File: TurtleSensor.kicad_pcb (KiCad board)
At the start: 2 copper layers, 72 x 72 mm, 10 parts, among them IC1 ATMEGA328-P, U1 HTU21DBreakout, U2 W25Q32FlashBreakout

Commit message: started routing
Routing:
- net +BATT: track 0.00 -> 114.0 mm
- net /SDA: track 0.00 -> 29.1 mm
- net /MOSI: track 0.00 -> 23.0 mm
- net /SCL: track 0.00 -> 18.5 mm
- net Net-(D1-Pad2): track 0.00 -> 15.7 mm
- net /MISO: track 0.00 -> 15.4 mm
- net /~CS: track 0.00 -> 14.4 mm
- net /SCK: track 0.00 -> 14.4 mm
- net Net-(22pF1-Pad2): track 0.00 -> 12.5 mm
- net Net-(22pF2-Pad2): track 0.00 -> 12.0 mm
- net Net-(D1-Pad1): track 0.00 -> 5.84 mm
- added copper zone on F.Cu, net GND
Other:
- net class Default: trace_width 0.25 -> 0.5
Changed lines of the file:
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@@
   (general
     (links 26)
-    (no_connects 26)
+    (no_connects 8)
     (area 97 79 170 152)
     (thickness 1.6)
     (drawings 4)
-    (tracks 0)
+    (tracks 56)
     (zones 0)
     (modules 10)
@@
   )
   (setup
-    (last_trace_width 0.25)
+    (last_trace_width 0.5)
     (trace_clearance 0.2)
     (zone_clearance 0.508)
@@
   (net_class Default "This is the default net class."
     (clearance 0.2)
-    (trace_width 0.25)
+    (trace_width 0.5)
     (via_dia 0.6)
     (via_drill 0.4)
@@
   (gr_line (start 170 152) (end 98 152) (angle 90) (layer Edge.Cuts) (width 0.1))
   (gr_line (start 170 80) (end 170 152) (angle 90) (layer Edge.Cuts) (width 0.1))
+  (segment (start 112 106.55906) (end 107.05906 106.55906) (width 0.25) (layer F.Cu) (net 1) (status 400000))
+  (segment (start 107.05906 106.55906) (end 106.5 106) (width 0.25) (layer F.Cu) (net 1) (status 800000))
+  (segment (start 118 108.32) (end 113.76094 108.32) (width 0.25) (layer F.Cu) (net 1) (status 400000))
+  (segment (start 113.76094 108.32) (end 112 106.55906) (width 0.25) (layer F.Cu) (net 1) (status 800000))
+  (segment (start 118 110.86) (end 112.58094 110.86) (width 0.25) (layer F.Cu) (net 2) (status 400000))
+  (segment (start 112.58094 110.86) (end 112 111.44094) (width 0.25) (layer F.Cu) (net 2) (status 800000))
+  (segment (start 112 111.44094) (end 107.05906 111.44094) (width 0.25) (layer F.Cu) (net 2) (status 400000))
+  (segment (start 107.05906 111.44094) (end 106.5 112) (width 0.25) (layer F.Cu) (net 2) (status 800000))
+  (segment (start 141 88) (end 141 87) (width 0.25) (layer F.Cu) (net 4) (status 400000))
+  (segment (start 111 83) (end 108 86) (width 0.25) (layer F.Cu) (net 4))
+  (segment (start 137 83) (end 111 83) (width 0.25) (layer F.Cu) (net 4))
+  (segment (start 141 87) (end 137 83) (width 0.25) (layer F.Cu) (net 4))
+  (segment (start 139 105) (end 143 105) (width 0.25) (layer F.Cu) (net 4))
+  (segment (start 135.68 108.32) (end 139 105) (width 0.25) (layer F.Cu) (net 4))
+  (segment (start 125.62 108.32) (end 135.68 108.32) (width 0.25) (layer F.Cu) (net 4) (status 400000))
+  (segment (start 142 121) (end 140 121) (width 0.25) (layer F.Cu) (net 4) (status 800000))
+  (segment (start 143 120) (end 142 121) (width 0.25) (layer F.Cu) (net 4))
+  (segment (start 143 105) (end 143 120) (width 0.25) (layer F.Cu) (net 4))
+  (segment (start 125.62 105.78) (end 125.62 108.32) (width 0.25) (layer F.Cu) (net 4) (status C00000))
+  (segment (start 118 103.24) (end 123.08 103.24) (width 0.25) (layer F.Cu) (net 4) (status 400000))
+  (segment (start 123.08 103.24) (end 125.62 105.78) (width 0.25) (layer F.Cu) (net 4) (status 800000))
+  (segment (start 115 97) (end 115 102) (width 0.25) (layer F.Cu) (net 4))
+  (segment (start 114 96) (end 115 97) (width 0.25) (layer F.Cu) (net 4))
+  (segment (start 112 96) (end 114 96) (width 0.25) (layer F.Cu) (net 4) (status 400000))
+  (segment (start 116.24 103.24) (end 115 102) (width 0.25) (layer F.Cu) (net 4))
+  (segment (start 116.24 103.24) (end 118 103.24) (width 0.25) (layer F.Cu) (net 4) (status 800000))
+  (segment (start 112 96) (end 112 88) (width 0.25) (layer F.Cu) (net 4) (status 400000))
+  (segment (start 110 86) (end 112 88) (width 0.25) (layer F.Cu) (net 4))
+  (segment (start 110 86) (end 108 86) (width 0.25) (layer F.Cu) (net 4))
+  (segment (start 108 86) (end 104 86) (width 0.25) (layer F.Cu) (net 4) (status 800000))
+  (segment (start 119 132) (end 124.84 132) (width 0.25) (layer F.Cu) (net 5) (status C00000))
+  (segment (start 125.62 121.02) (end 123.98 121.02) (width 0.25) (layer F.Cu) (net 6) (status 400000))
+  (segment (start 116.46 128.54) (end 116.46 132) (width 0.25) (layer F.Cu) (net 6) (status 800000))
+  (segment (start 123.98 121.02) (end 116.46 128.54) (width 0.25) (layer F.Cu) (net 6))
+  (segment (start 125.62 118.48) (end 139.98 118.48) (width 0.25) (layer F.Cu) (net 17) (status C00000))
+  (segment (start 139.98 118.48) (end 140 118.46) (width 0.25) (layer F.Cu) (net 17) (status C00000))
+  (segment (start 125.62 115.94) (end 123.94 115.94) (width 0.25) (layer F.Cu) (net 18) (status 400000))
+  (segment (start 138.62 112) (end 140 113.38) (width 0.25) (layer F.Cu) (net 18) (status 800000))
+  (segment (start 124 112) (end 138.62 112) (width 0.25) (layer F.Cu) (net 18))
+  (segment (start 123 113) (end 124 112) (width 0.25) (layer F.Cu) (net 18))
+  (segment (start 123 115) (end 123 113) (width 0.25) (layer F.Cu) (net 18))
+  (segment (start 123.94 115.94) (end 123 115) (width 0.25) (layer F.Cu) (net 18))
+  (segment (start 140 115.92) (end 132.92 115.92) (width 0.25) (layer F.Cu) (net 19) (status 400000))
+  (segment (start 130.4 113.4) (end 125.62 113.4) (width 0.25) (layer F.Cu) (net 19) (status 800000))
+  (segment (start 132.92 115.92) (end 130.4 113.4) (width 0.25) (layer F.Cu) (net 19))
+  (segment (start 125.62 110.86) (end 139.98 110.86) (width 0.25) (layer F.Cu) (net 20) (status C00000))
+  (segment (start 139.98 110.86) (end 140 110.84) (width 0.25) (layer F.Cu) (net 20) (status C00000))
+  (segment (start 141 93.08) (end 143.08 93.08) (width 0.25) (layer F.Cu) (net 25) (status 400000))
+  (segment (start 134.08 99) (end 125.62 90.54) (width 0.25) (layer F.Cu) (net 25) (status 800000))
+  (segment (start 142 99) (end 134.08 99) (width 0.25) (layer F.Cu) (net 25))
+  (segment (start 144 97) (end 142 99) (width 0.25) (layer F.Cu) (net 25))
+  (segment (start 144 94) (end 144 97) (width 0.25) (layer F.Cu) (net 25))
+  (segment (start 143.08 93.08) (end 144 94) (width 0.25) (layer F.Cu) (net 25))
+  (segment (start 125.62 88) (end 129 88) (width 0.25) (layer F.Cu) (net 26) (status 400000))
+  (segment (start 136.62 95.62) (end 141 95.62) (width 0.25) (layer F.Cu) (net 26) (status 800000))
+  (segment (start 129 88) (end 136.62 95.62) (width 0.25) (layer F.Cu) (net 26))
+  (zone (net 3) (net_name GND) (layer F.Cu) (hatch edge 0.508)
+    (connect_pads (clearance 0.508))
+    (min_thickness 0.254)
+    (fill (arc_segments 16) (thermal_gap 0.508) (thermal_bridge_width 0.508))
+    (polygon
+      (pts
+        (xy 158 82) (xy 159 103) (xy 159 141) (xy 98 142) (xy 98 80)
+        (xy 151 80) (xy 158 82)
+      )
+    )
+  )
 )

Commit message: before new pcb
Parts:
- added J1: ISPConnector, Socket_Strips:Socket_Strip_Straight_2x03, F.Cu at (146.0, 135.0)

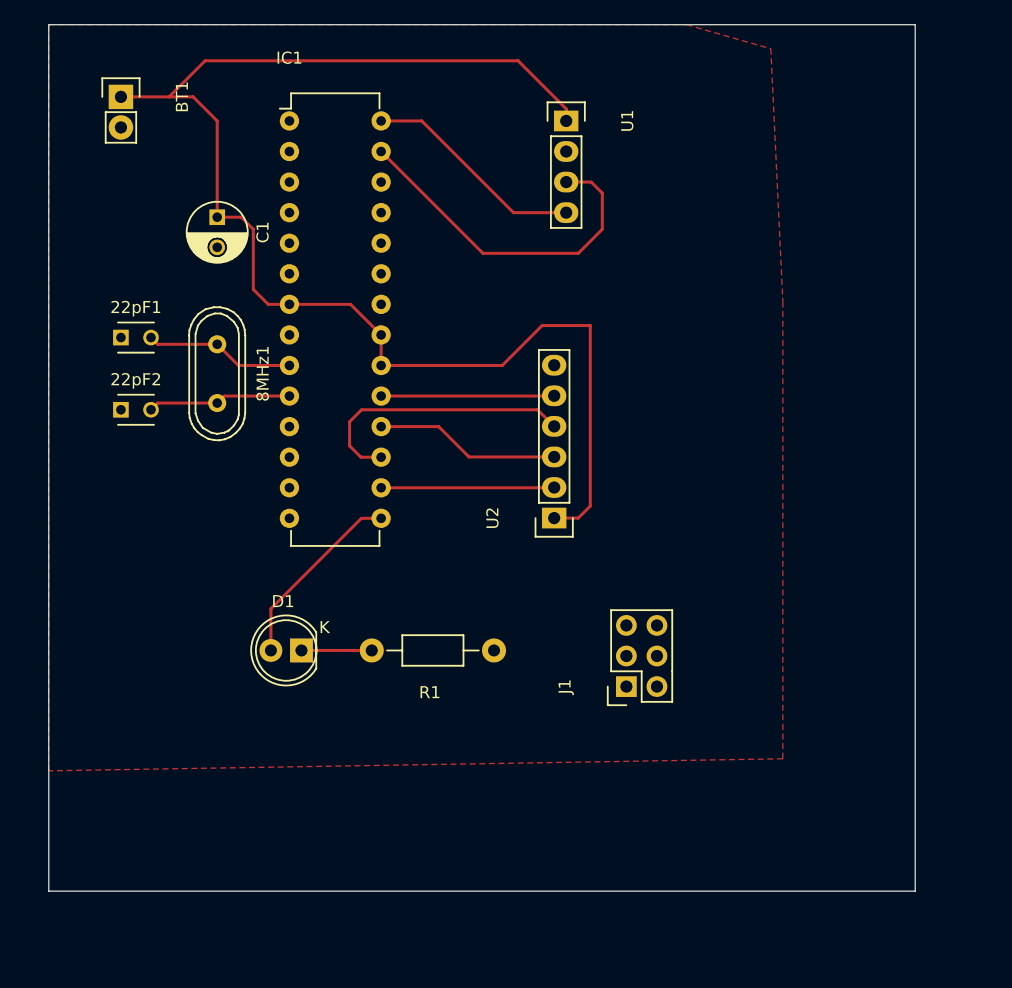
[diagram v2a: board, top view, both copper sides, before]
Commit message: routed pcb rev 0.1
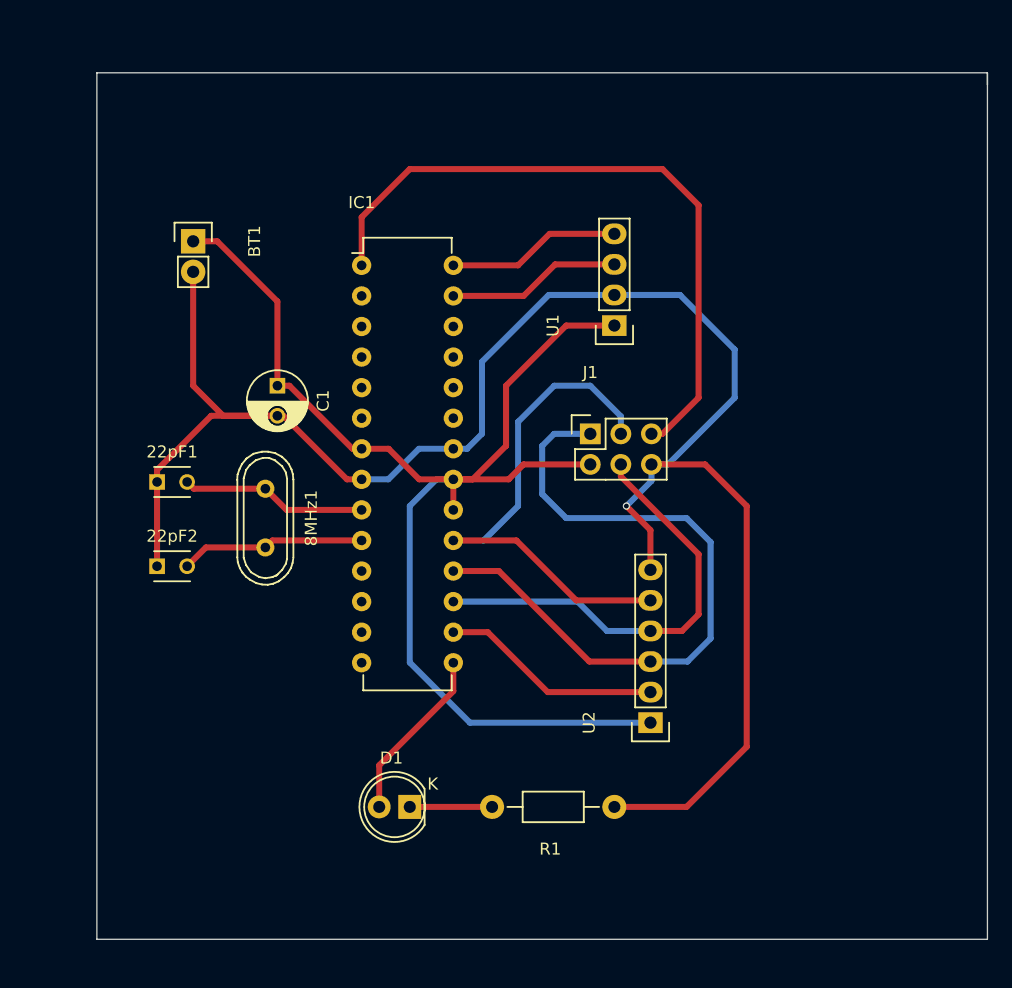
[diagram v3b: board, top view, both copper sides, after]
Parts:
- moved J1 21.2 mm to (143.0, 114.0), turned to 0 degrees
- moved U2 18.8 mm to (148.0, 138.0)
- moved U1 17.5 mm to (145.0, 105.0), turned to 90 degrees
- moved R1 16.4 mm to (145.0, 145.0)
- moved D1 15.8 mm to (128.0, 145.0)
- moved C1 14.9 mm to (117.0, 110.0)
- moved BT1 13.4 mm to (110.0, 98.0)
- moved IC1 13.4 mm to (124.0, 100.0)
- moved 22pF2 13.3 mm to (107.0, 125.0)
- moved 8MHz1 12.6 mm to (116.0, 121.0)
- moved 22pF1 12.4 mm to (107.0, 118.0)
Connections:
- IC1 pad 1: Net-(IC1-Pad1) -> /~RST
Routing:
- net GND: track 0.00 -> 155.4 mm, vias 0 -> 1
- net /~RST: track 0.00 -> 56.1 mm
- net /MISO: track 15.4 -> 57.4 mm
- net /SCK: track 14.4 -> 44.3 mm
- net /SDA: track 29.1 -> 14.5 mm
- net /MOSI: track 23.0 -> 37.1 mm
- net +BATT: track 114.0 -> 109.6 mm
- net /SCL: track 18.5 -> 14.5 mm
- net /~CS: track 14.4 -> 18.4 mm
- net Net-(22pF2-Pad2): track 12.0 -> 15.4 mm
- net Net-(22pF1-Pad2): track 12.5 -> 15.5 mm
- net Net-(D1-Pad2): track 15.7 -> 14.5 mm
- net Net-(D1-Pad1): track 5.84 -> 6.84 mm
- removed copper zone on F.Cu, net GND
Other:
- board size 72 x 72 mm -> 74 x 72 mm

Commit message: update component positioning
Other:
- board size 74 x 72 mm -> 72 x 72 mm
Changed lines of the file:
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@@
     (area 101.949999 83.949999 176.050001 156.050001)
     (thickness 1.6)
-    (drawings 5)
+    (drawings 4)
     (tracks 114)
     (zones 0)
@@
     )
   )
-  (gr_line (start 176 84) (end 176 85) (angle 90) (layer Edge.Cuts) (width 0.1))
-  (gr_line (start 102 84) (end 176 84) (angle 90) (layer Edge.Cuts) (width 0.1))
-  (gr_line (start 102 156) (end 102 84) (angle 90) (layer Edge.Cuts) (width 0.1))
-  (gr_line (start 176 156) (end 102 156) (angle 90) (layer Edge.Cuts) (width 0.1))
-  (gr_line (start 176 84) (end 176 156) (angle 90) (layer Edge.Cuts) (width 0.1))
+  (gr_line (start 168 158) (end 96 158) (angle 90) (layer Edge.Cuts) (width 0.1))
+  (gr_line (start 168 86) (end 168 158) (angle 90) (layer Edge.Cuts) (width 0.1))
+  (gr_line (start 96 86) (end 168 86) (angle 90) (layer Edge.Cuts) (width 0.1))
+  (gr_line (start 96 158) (end 96 86) (angle 90) (layer Edge.Cuts) (width 0.1))
   (segment (start 116 118.55906) (end 110.05906 118.55906) (width 0.5) (layer F.Cu) (net 1))
   (segment (start 110.05906 118.55906) (end 109.5 118) (width 0.5) (layer F.Cu) (net 1))
